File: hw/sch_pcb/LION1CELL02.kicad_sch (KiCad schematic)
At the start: 82 parts, among them IC1 BQ294602DRVR, J1 CONN1_1, J10 JUMP_2x1, J11 JUMP_2x1, J12 JUMP_2x1, J13 JUMP_2x1, J2 CONN1_1, J3 Jack-DC, J4 JUMP_2x1, J5 JUMP_2x1, J6 JUMP_2x1, J7 JUMP_2x1, J8 JUMP2_2x1, J9 Conn_02x03_Odd_Even, M1 HOLE M3, M2 HOLE M3, M3 HOLE, M4 HOLE, Q1 IRLML6244, SW1 SW_PUSH, U1 BQ24103, U2 SN74HC164D, U3 BQ34Z100

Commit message: Update schematics
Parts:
- removed BT1: lion, symbol Device:Battery_Cell
- removed C1, C14, C5: 100nF, Mlab_C:SMD-0805, symbol Device:C
- removed C10, C11, C13, C3, C4, C6, C7, C9: 100nF, Mlab_C:SMD-0805, symbol LION2CELL01D-rescue:C-RESCUE-LION2CELL01C
- removed C12: 1uF, Mlab_C:SMD-0805, symbol LION2CELL01D-rescue:C-RESCUE-LION2CELL01C
- removed C15: 100nF, Mlab_R:SMD-0805, symbol LION2CELL01D-rescue:C-RESCUE-LION2CELL01C
- removed C2: 10uF, Mlab_C:TantalC_SizeD_Reflow, symbol Device:C_Polarized
- removed C8: 10uF, Mlab_C:TantalC_SizeD_Reflow, symbol LION2CELL01D-rescue:CP2
- removed D1: M4, Mlab_D:SMA_Standard, symbol LION2CELL01D-rescue:DIODE
- removed D10, D11, D12, D13, D14, D7, D8, D9: ORAGE, Mlab_D:LED_1206, symbol LION2CELL01D-rescue:LED-RESCUE-LION2CELL01C
- removed D2: M4, symbol Device:D
- removed D3, D4: Green, Mlab_D:LED_1206, symbol LION2CELL01D-rescue:LED-RESCUE-LION2CELL01C
- removed D5: Red, Mlab_D:LED_1206, symbol LION2CELL01D-rescue:LED-RESCUE-LION2CELL01C
- removed D6: ZSMD-5V6, symbol Device:D_Zener
- removed IC1: BQ294602DRVR, symbol BQ294602DRVR:BQ294602DRVR
- removed J10, J11, J12, J13, J4, J5, J6, J7: JUMP_2x1, Mlab_Pin_Headers:Straight_1x02, symbol LION2CELL01D-rescue:JUMP_2x1
- removed J3: Jack-DC, symbol Connector:Jack-DC
- removed J8: JUMP2_2x1, symbol LION2CELL01D-rescue:JUMP2_2x1
- removed L1: DE1205-10, Mlab_L:DE1205-10, symbol LION2CELL01D-rescue:INDUCTOR_SMALL
- removed M1, M2: HOLE M3, Mlab_Mechanical:MountingHole_3mm, symbol mlab-default-rescue:HOLE
- removed M3, M4: HOLE, Mlab_Mechanical:MountingHole_3mm, symbol mlab-default-rescue:HOLE
- removed Q1: IRLML6244, Mlab_T:SOT-23, symbol LION2CELL01D-rescue:MOSFET-N
- removed R1, R7: 7k5, symbol Device:R
- removed R10: 9K31, Mlab_R:SMD-0805, symbol LION2CELL01D-rescue:R-RESCUE-LION2CELL01C
- removed R11: 442K, Mlab_R:SMD-0805, symbol LION2CELL01D-rescue:R-RESCUE-LION2CELL01C
- removed R12: 0R1, Resistors_SMD:R_2512, symbol LION2CELL01D-rescue:R-RESCUE-LION2CELL01C
- removed R13, R14, R15, R16, R17, R18, R19, R20, R4, R5, R6: 270R, Mlab_R:SMD-0805, symbol LION2CELL01D-rescue:R-RESCUE-LION2CELL01C
- removed R2, R3: 10k, Mlab_R:SMD-0805, symbol LION2CELL01D-rescue:R-RESCUE-LION2CELL01C
- removed R21: 1K, Mlab_R:SMD-0805, symbol LION2CELL01D-rescue:R-RESCUE-LION2CELL01C
- removed R22, R23: 100R, Mlab_R:SMD-0805, symbol LION2CELL01D-rescue:R-RESCUE-LION2CELL01C
- removed R24: 0R01 75PPM, Mlab_R:SMD-2512, symbol LION2CELL01D-rescue:R-RESCUE-LION2CELL01C
- removed R8, R9: 7K5, Mlab_R:SMD-0805, symbol LION2CELL01D-rescue:R-RESCUE-LION2CELL01C
- removed SW1: SW_PUSH, Mlab_SW:SW_PUSH_SMALL, symbol LION2CELL01D-rescue:SW_PUSH
- removed TH1, TH2: NCP21XV103J03RA, symbol Device:Thermistor
- removed U1: BQ24103, Mlab_IO:VQFN-20, symbol LION2CELL01D-rescue:BQ24103
- removed U2: SN74HC164D, Mlab_IO:SO-14, symbol LION2CELL01D-rescue:SN74HC164D
- removed U3: BQ34Z100, Mlab_IO:TSSOP-14_4.4x5mm_Pitch0.65mm, symbol LION2CELL01D-rescue:BQ34Z100
- added BT1: BATT, Mlab_Batery:BAT_BK-18650-PC4, symbol MLAB_BATERY:2xBATT
- added C10, C36: 22u, Capacitor_SMD:C_0805_2012Metric, symbol Device:C_Small
- added C11: 4u7, Capacitor_SMD:C_0805_2012Metric, symbol Device:C_Small
- added C18: 100n, symbol Device:C
- added C25, C26, C29, C30, C6: 100n, Capacitor_SMD:C_0805_2012Metric, symbol Device:C_Small
- added C31, C7: 1u, Capacitor_SMD:C_0805_2012Metric, symbol Device:C_Small
- added C34: 3n3, Capacitor_SMD:C_0805_2012Metric, symbol Device:C_Small
- added C39: 47u, Capacitor_SMD:C_0805_2012Metric, symbol Device:C_Small
- added C4: 100nF, Capacitor_SMD:C_0805_2012Metric, symbol Device:C_Small
- added C42, C5, C9: 10u, Capacitor_SMD:C_0805_2012Metric, symbol Device:C_Small
- added C53: 1n, Capacitor_SMD:C_0805_2012Metric, symbol Device:C_Small
- added C8: 47n, Capacitor_SMD:C_0805_2012Metric, symbol Device:C_Small
- added D1, D4, D5: ORANGE, Mlab_D:SMD_LED_RIGHT_KINGBRIGHT_1605, symbol Device:LED_Small
- added D10, D6, D7, D8, D9: GREEN, Mlab_D:SMD_LED_RIGHT_KINGBRIGHT_1605, symbol Device:LED_Small
- added D2, D3: RED, Mlab_D:SMD_LED_RIGHT_KINGBRIGHT_1605, symbol Device:LED_Small
- added FID1, FID2, FID3, FID4: Fiducial, Fiducial:Fiducial_1mm_Mask2mm, symbol Mechanical:Fiducial
- added H1, H2, H3, H4: M3, Mlab_Mechanical:MountingHole_3mm, symbol Mechanical:MountingHole_Pad
- added J1: USBC_USB4105-GF-A, Mlab_CON:USBC GCT_USB4105-GF-A, symbol MLAB_CONNECTORS:USBC_USB4105-GF-A
- added J9: JUMP_4X2, symbol MLAB_Jumpers:JUMP_4X2
- added JP5: Jumper_3_Bridged12, Jumper:SolderJumper-3_P1.3mm_Bridged2Bar12_RoundedPad1.0x1.5mm, symbol Jumper:SolderJumper_3_Bridged12
- added L1, L2: 1uH - DFE252012P-1R0M=P2, Inductor_SMD:L_1008_2520Metric, symbol Device:L
- added NT1, NT2: NetTie_2, NetTie:NetTie-2_SMD_Pad0.5mm, symbol Device:NetTie_2
- added Q1, Q2: DMN1029UFDB-7, symbol Transistor_FET:Q_NMOS_GDS
- added Q4: BSS83P, Package_TO_SOT_SMD:SOT-23, symbol Device:Q_PMOS_GSD
- added Q5, Q6: BC807-25, Package_TO_SOT_SMD:SOT-23-3, symbol Device:Q_PNP_BEC
- added R1, R2, R21: 5k1, Resistor_SMD:R_0805_2012Metric, symbol Device:R_Small
- added R10, R11, R12, R13, R19, R50: 270R, Resistor_SMD:R_0805_2012Metric, symbol Device:R_Small
- added R14, R15, R16, R17, R51: 68R, Resistor_SMD:R_0805_2012Metric, symbol Device:R_Small
- added R18: 2k4, Resistor_SMD:R_0805_2012Metric, symbol Device:R_Small
- added R20, R48, R49: 1k, Resistor_SMD:R_0805_2012Metric, symbol Device:R_Small
- added R22: 33k, Resistor_SMD:R_0805_2012Metric, symbol Device:R_Small
- added R27: 330, symbol Device:R
- added R28: 2k2, symbol Device:R
- added R3: 0R01 75PPM, Resistor_SMD:R_2512_6332Metric, symbol Device:R_Small
- added R5, R6: 4M7, Resistor_SMD:R_0805_2012Metric, symbol Device:R_Small
- added R59, R60: 100R, Resistor_SMD:R_0805_2012Metric, symbol Device:R_Small
- added R75: 511k, Resistor_SMD:R_0805_2012Metric, symbol Device:R_Small
- added R76: 91k, Resistor_SMD:R_0805_2012Metric, symbol Device:R_Small
- added R8: R, Resistor_SMD:R_0805_2012Metric, symbol Device:R_Small
- added R9: 510R, Resistor_SMD:R_0805_2012Metric, symbol Device:R_Small
- added SW3: SKRTLAE010, Mlab_SW:SKRT, symbol MLAB_SW:SW_Push_shield
- added TH1: 10k NTC, Resistor_SMD:R_0805_2012Metric, symbol Device:Thermistor_NTC
- added TH3: 10k NTC, Resistor_SMD:R_0805_2012Metric, symbol Device:Thermistor
- added U1: BQ29700DSER, Package_SON:WSON-6_1.5x1.5mm_P0.5mm, symbol Battery_Management:BQ297xy
- added U15: TPS631000DRLR, Package_TO_SOT_SMD:SOT-583-8, symbol MLAB_U:TPS631000DRLR
- added U2: SN74HC164P, Package_SO:TSSOP-14_4.4x5mm_P0.65mm, symbol MLAB_IO:SN74HC164D
- added U3: BQ25628E, Mlab_IO:Texas_S-WQFN-HR-18, symbol MLAB_IO:BQ25628E
- added U5: BQ34Z100, Mlab_IO:TSSOP-14_4.4x5mm_Pitch0.65mm, symbol MLAB_IO:BQ34Z100
- F1: value 3A -> Fuse; footprint (none) -> Fuse:Fuseholder_Littelfuse_Nano2_154x; UST_ID (none) -> 5c70984512875079b91f88d8
- F2: value 1.1A -> Fuse; footprint (none) -> Fuse:Fuseholder_Littelfuse_Nano2_154x; UST_ID (none) -> 5c70984512875079b91f88d8
- renumbered J1 to J2, J2 to J3, J9 to J4
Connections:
- net BAT+: no longer F1.2
- net GND: now also C10.2, C11.2, C18.2, C25.2, C29.2, C30.2, C31.2, C34.2, C36.2, C39.2, C4.2, C42.2, C5.2, C53.2, C6.2, C7.2, C9.2, D1.1 (K), D10.1 (K), H1.1, H2.1, H3.1, H4.1, J1.A1/B12 (GND), J1.B1/A12 (GND), J1.G1 (SHIELD), J1.G2 (SHIELD), J1.G3 (SHIELD), J1.G4 (SHIELD), J9.1 (2), J9.2, NT2.2, Q2.3 (S), R1.1, R18.2, R2.1, R20.1, R28.2, R3.2, R6.1, R76.2, U1.4 (VSS), U15.6 (MODE), U15.7 (GND), U2.7 (GND), U3.14 (~{CE}), U3.15 (GND), U5.8 (VSS)
- net HDQ: now also J9.3 (4), J9.4, U5.12 (P5/HDQ)
- net P1: now also U2.1 (A), U2.2 (B), U5.3 (P1)
- net P2: now also U2.8 (CLK), U5.1 (P2)
- net SCL: now also J9.5, J9.6 (5), U3.13 (SCL), U5.13 (P4/SCL)
- net SDA: now also J9.7 (8), J9.8, U3.12 (SDA), U5.14 (P3/SDA)
- net at F2.2: now also BT1.2+ (+)
- net +BATT: now reaches F2.1
- net +BATT: now also F1.1, C34.1, C9.1, JP5.3 (B), Q1.3 (S), R27.1, R5.1, U3.8 (BAT), U5.4 (BAT)
- new net: J1.B5 (CC2), R1.2
- new net: D6.1 (K), R14.1
- new net: C26.2, C30.1, R60.2, U5.10 (SRN)
- new net: Q5.3 (C), R51.1
- new net: D10.2 (A), R51.2
- new net: D7.1 (K), R15.1
- new net: BT1.1+ (+), F1.2
- new net: Q5.1 (B), R49.2
- new net: C25.1, JP5.2 (C), U5.5 (CE), U5.6 (REGIN)
- new net: D9.1 (K), R17.1
- new net: C7.1, R18.1, U3.4 (ILIM)
- new net: L2.1, U15.3 (LX1)
- new net: L2.2, U15.2 (LX2)
- new net: C8.1, L1.1, U3.16 (SW)
- new net: C8.2, U3.1 (BTST)
- new net: C26.1, C29.1, R59.2, U5.9 (SRP)
- new net: R21.1, U3.5 (TS_BIAS)
- new net: R21.2, R22.1, TH1.1, U3.6 (TS)
- new net: Q2.1 (G), R6.2, U1.3 (Dout)
- new net: C31.1, TH3.1, U5.7 (REG25)
- new net: Q1.1 (G), R5.2, U1.2 (Cout)
- new net: Q1.2 (D), Q2.2 (D)
- new net: Q6.1 (B), R48.2
- new net: TH3.2, U5.11 (P6/TS)
- new net: Q4.1 (G), R9.2
- new net: Q4.3 (D), R19.2
- new net: D5.1 (K), R13.1
- new net: C18.1, R27.2, U1.5 (BAT)
- new net: D4.1 (K), R12.1
- new net: D2.1 (K), R10.1
- new net: R28.1, U1.6 (V-)
- new net: J1.A5 (CC1), R2.2
- new net: R22.2, TH1.2
- new net: D3.1 (K), R11.1
- new net: C5.1, C6.1, U3.17 (PMID)
- new net: C11.1, U3.2 (REGN)
- new net: D1.2 (A), R50.2
- new net: J1.A6 (D+), J1.B6 (D+)
- new net: D8.1 (K), R16.1
- new net: Q6.3 (C), R50.1
- new net +3.3V: C39.1, C4.1, C42.1, D2.2 (A), D3.2 (A), D4.2 (A), D5.2 (A), D6.2 (A), D7.2 (A), D8.2 (A), D9.2 (A), JP5.1 (A), Q4.2 (S), Q5.2 (E), Q6.2 (E), R75.1, R8.2, U15.1 (VOUT), U2.14 (VCC), U2.9 (CLR)
- new net +VSW: C10.1, C36.1, L1.2, U15.4 (VIN), U15.5 (EN), U3.9 (SYS)
- new net 3v3i_FB: R75.2, R76.1, U15.8 (FB)
- new net A: R10.2, U2.3 (QA)
- new net B: R11.2, U2.4 (QB)
- new net BAT-: BT1.1- (-), BT1.2- (-), NT1.2, R3.1
- new net C: R12.2, U2.5 (QC)
- new net CH_PG: R49.1, U3.3 (~{PG})
- new net CH_STAT: R48.1, U3.10 (STAT)
- new net D: R13.2, U2.6 (QD)
- new net E: R14.2, U2.10 (QE)
- new net EXT_DETECTION_CHARGER: R8.1, R9.1, SW3.1, U3.7 (~{QON})
- new net F: R15.2, U2.11 (QF)
- new net G: R16.2, U2.12 (QG)
- new net GAUGE_BTN_IN: R19.1, R20.2, U5.2 (VEN)
- new net GAUGE_SRN: NT2.1, R60.1
- new net GAUGE_SRP: NT1.1, R59.1
- new net H: R17.2, U2.13 (QH)
- new net VBUS: C53.1, J1.A4/B9 (VBUS), J1.B4/A9 (VBUS), U3.18 (VBUS)
- no-connect marks 0 -> 3
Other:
- note added: "+3.3V"
- note added: "0%"
- note added: "100%"
- note added: "GREEN"
- note added: "Need to obtain 2.5V, here"
- note added: "ORANGE"
- note added: "RED"
- note removed: "MOUNTING HOLES"
- note removed: "TO HOST MCU"
- moved on the sheet: J2, J3, J4

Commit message: Update schematics
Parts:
- removed C18: 100n, symbol Device:C
- removed J2, J3: CONN1_1, Mlab_Con:WAGO256, symbol LION2CELL01D-rescue:CONN1_1
- removed J4: Conn_02x03_Odd_Even, symbol Connector_Generic:Conn_02x03_Odd_Even
- removed J9: JUMP_4X2, symbol MLAB_Jumpers:JUMP_4X2
- removed R27: 330, symbol Device:R
- removed R8: R, Resistor_SMD:R_0805_2012Metric, symbol Device:R_Small
- removed SW3: SKRTLAE010, Mlab_SW:SKRT, symbol MLAB_SW:SW_Push_shield
- added C7: 100n, Capacitor_SMD:C_0805_2012Metric, symbol Device:C_Small
- added J2: HEADER_2x03, Connector_PinHeader_2.54mm:PinHeader_2x03_P2.54mm_Vertical, symbol MLAB_HEADER:HEADER_2x03
- added J3: HEADER_1x04, Connector_PinHeader_2.54mm:PinHeader_1x04_P2.54mm_Horizontal, symbol MLAB_HEADER:HEADER_1x04
- added R11: 330, symbol Device:R_Small
- added R30, R31: 4k7, Resistor_SMD:R_0805_2012Metric, symbol Device:R_Small
- added SW1: SKRTLAE010, Mlab_SW:SKRT, symbol MLAB_SW:SW_Push_shield
- C13: renamed from C4; value 100nF -> 100n
- R12: renamed from R28; footprint (none) -> Resistor_SMD:R_0805_2012Metric
- renumbered C36 to C1, C9 to C10, C10 to C11, C11 to C12, C25 to C14, C26 to C15, C29 to C16, C30 to C17, C31 to C18, C34 to C19, C39 to C2, C53 to C3, C42 to C4, C7 to C8, C8 to C9, D9 to D10, D10 to D2, D2 to D3, D3 to D4, D4 to D5, D5 to D6, D6 to D7, D7 to D8, D8 to D9, JP5 to JP1, L2 to L1, L1 to L2, Q6 to Q1, Q5 to Q2, Q4 to Q3, Q1 to Q4, Q2 to Q5, R9 to R10, R19 to R13, R20 to R14, R18 to R15, R21 to R16, R22 to R17, R5 to R18, R6 to R19, R10 to R20, R11 to R21, R12 to R22, R13 to R23, R14 to R24, R15 to R25, R16 to R26, R17 to R27, R59 to R28, R60 to R29, R75 to R3, R76 to R4, R48 to R5, R49 to R6, R50 to R7, R51 to R8, R3 to R9, TH3 to TH2, U15 to U1, U3 to U2, U1 to U3, U5 to U4, U2 to U5
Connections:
- net +3.3V: now also J3.4, R30.2, R31.2
- net +BATT: now also J2.3, J2.4, R11.1
- net GND: now also C7.2, J2.1, J2.2, J2.5, J2.6, J3.1, SW1.2, SW1.GND (SHIELD)
- net SCL: now also J3.3, R30.1
- net SDA: now also J3.2, R31.1
- net at U3.5 (BAT): now also C7.1, R11.2
- net at J1.A6 (D+): no longer J1.B6 (D+)
- net EXT_DETECTION_CHARGER renamed RESET
- net RESET: now also SW1.1
- net HDQ: no longer names the net of U4.12 (P5/HDQ)
- no-connect marks 3 -> 8
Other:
- note added: "BUCK CONVERTER"
- note added: "I2C"
- note added: "MOUNTING HOLES"
- note added: "POWER OUT"
- note added: "UI"
- note added: "USB-C"
- note removed: "POWER OUTPUT"
- moved on the sheet: BT1A, BT1B, C1, C10, C11, C12, C13, C14, C15, C16, C17, C18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

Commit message: Repository cleanup.
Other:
- company: Mlab.cz -> MLAB.cz
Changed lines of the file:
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@@
 		(title "LION1CELL02A")
 		(date "2024-07-17")
-		(company "Mlab.cz")
+		(company "MLAB.cz")
 		(comment 1 "Singe cell Li-ion battery management\\nwith USB-C charger")
 	)

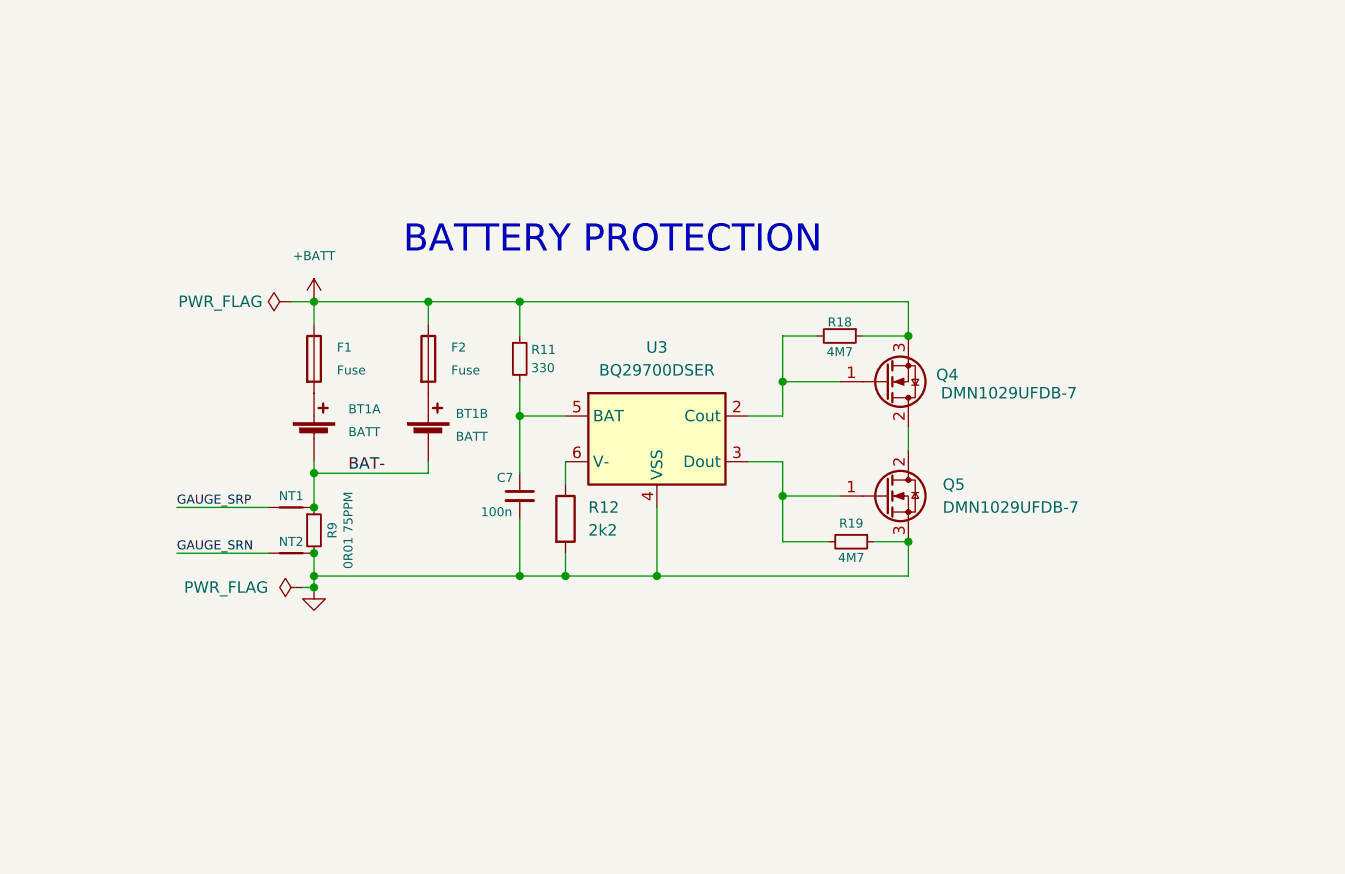
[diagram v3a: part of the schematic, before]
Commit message: Batery protection update
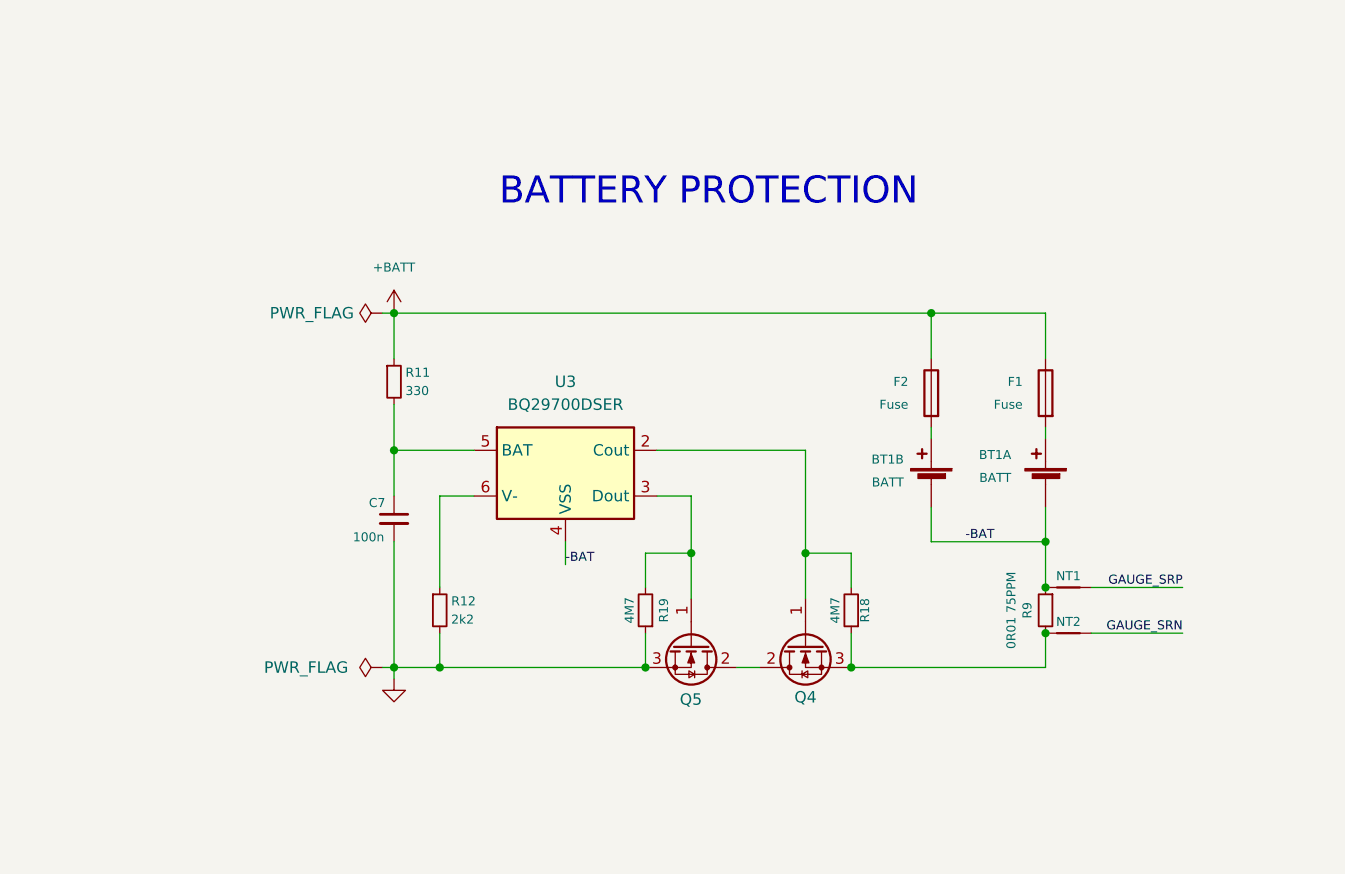
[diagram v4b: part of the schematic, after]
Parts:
- removed R12: 2k2, Resistor_SMD:R_0805_2012Metric, symbol Device:R
- added R12: 2k2, symbol Device:R_Small
- Q4, Q5: value DMN1029UFDB-7 -> ~
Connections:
- net +BATT: no longer Q4.3 (S), R18.1
- net GND: now also R12.2; no longer NT2.2, R9.2, U3.4 (VSS)
- net at U3.6 (V-): now also R12.1
- net BAT- renamed -BAT
- net -BAT: now also U3.4 (VSS)
- new net: NT2.2, Q4.3 (S), R18.1, R9.2
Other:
- moved on the sheet: BT1A, BT1B, C7, F1, F2, NT1, NT2, Q4, Q5, R11, R18, R19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

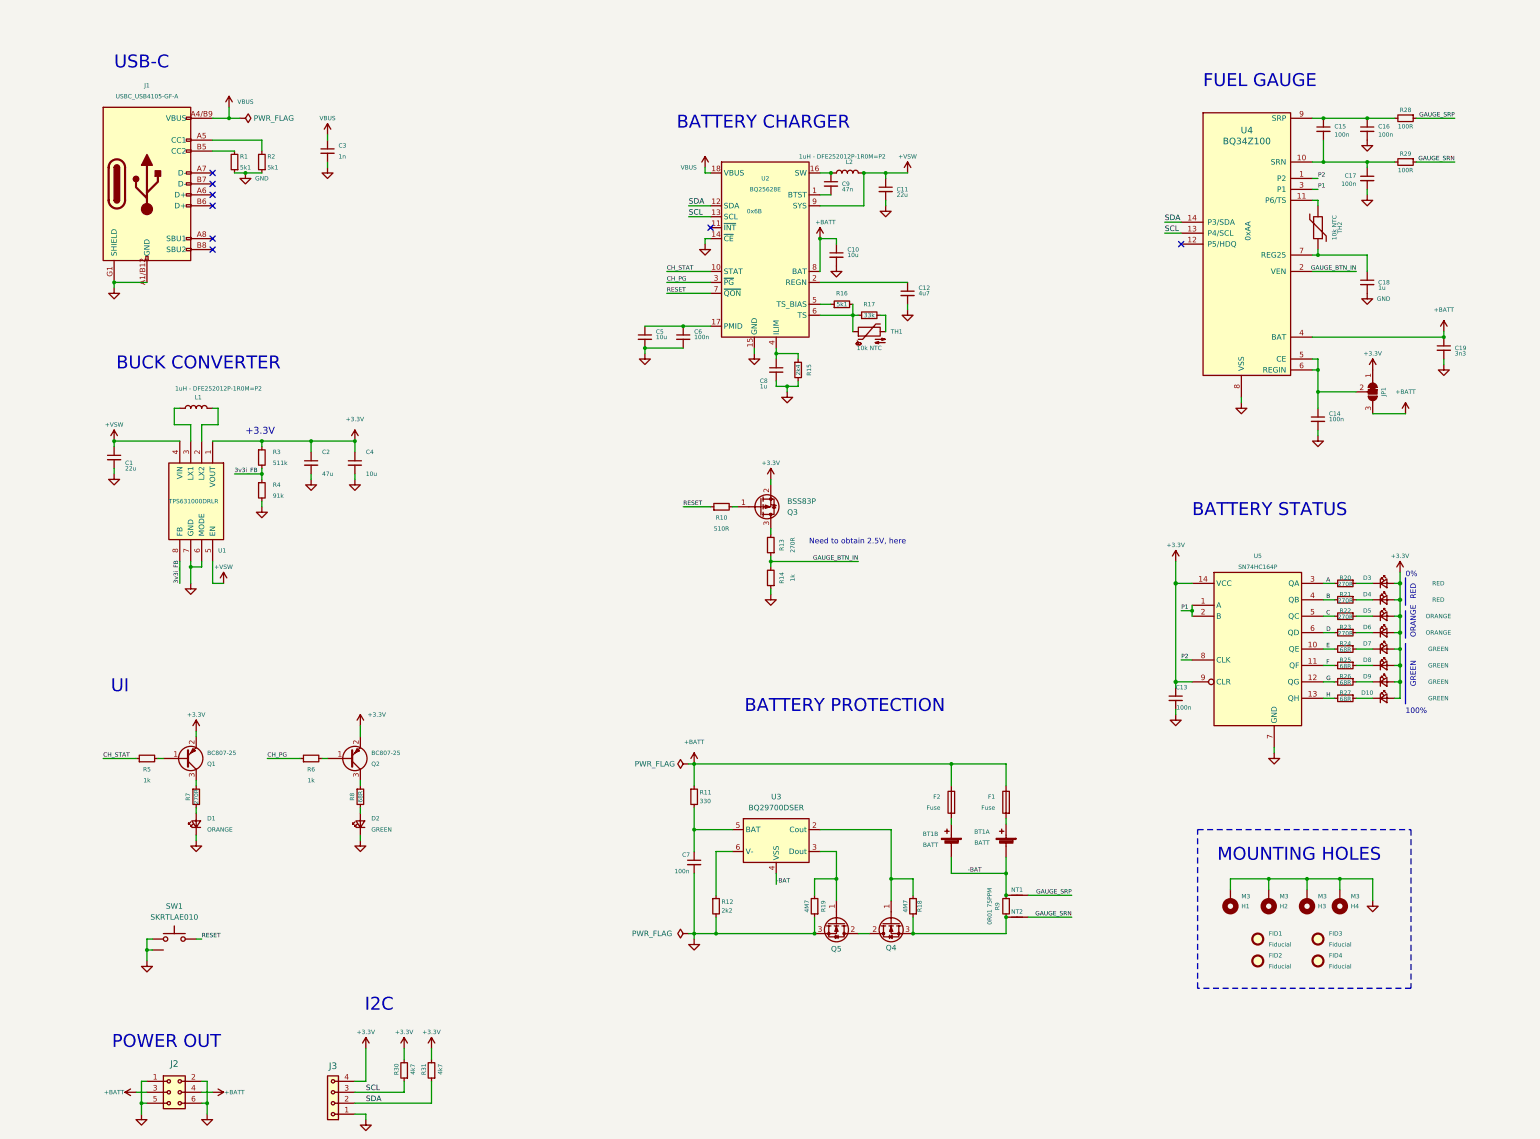
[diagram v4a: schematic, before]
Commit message: Battery pack update
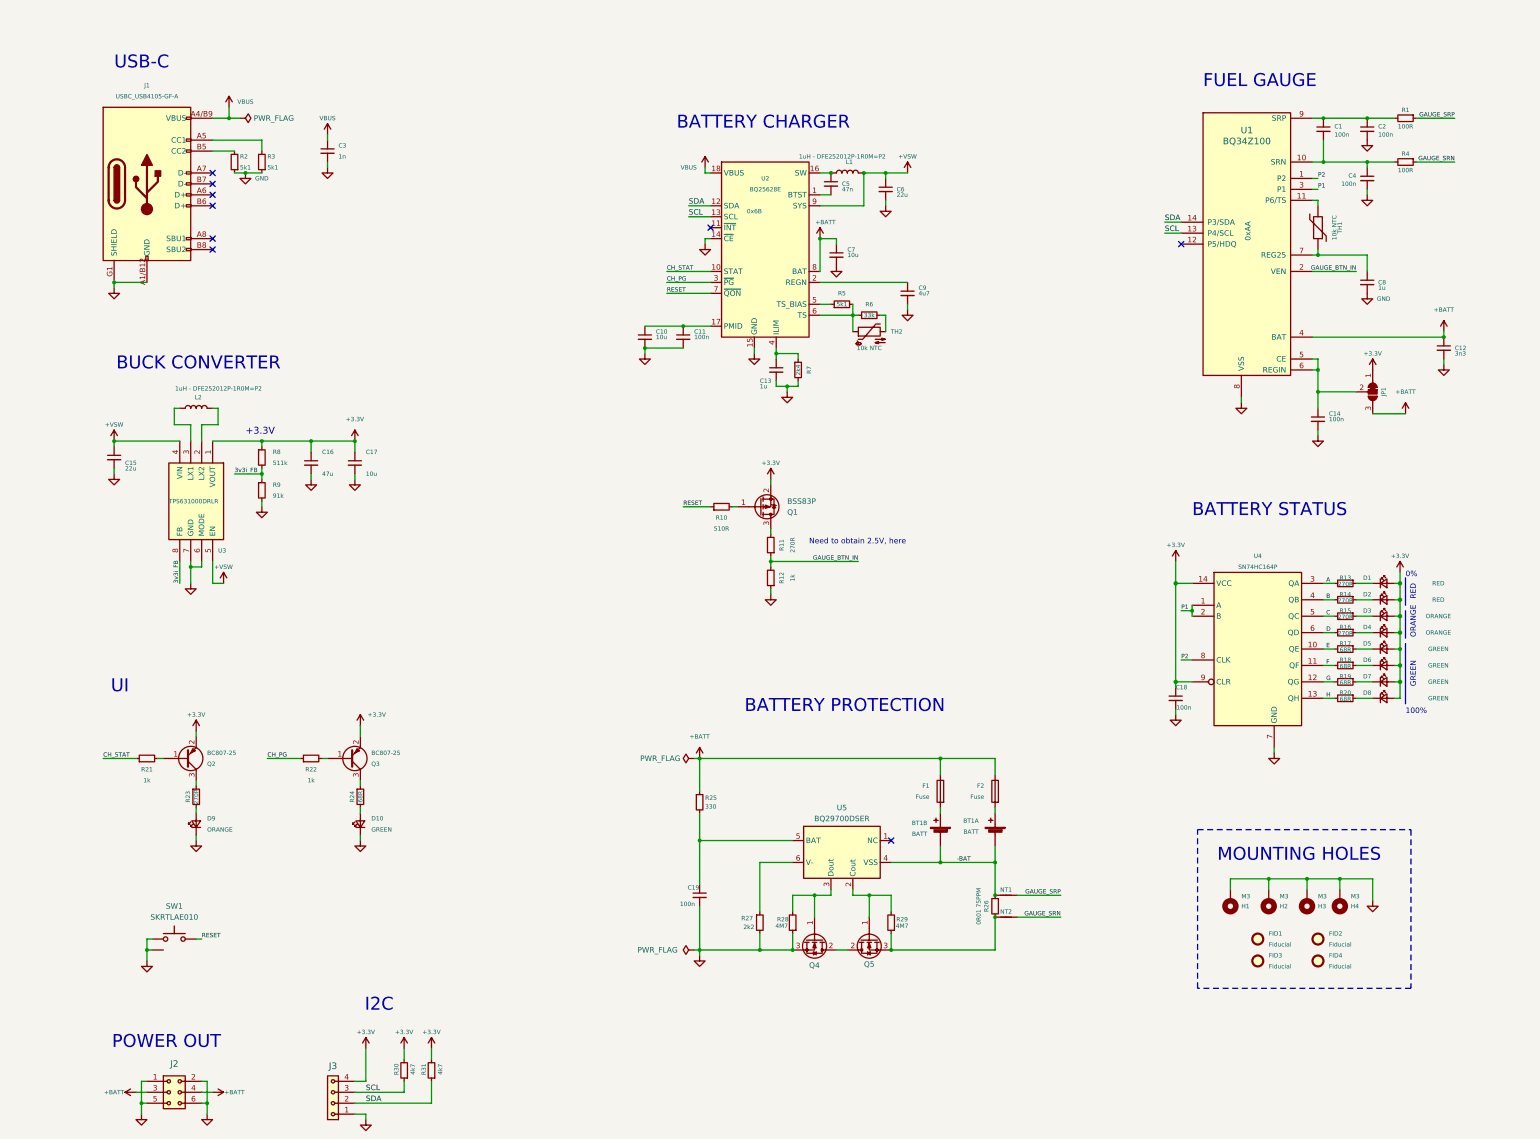
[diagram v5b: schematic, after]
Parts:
- renumbered C15 to C1, C5 to C10, C6 to C11, C19 to C12, C8 to C13, C1 to C15, C2 to C16, C4 to C17, C13 to C18, C7 to C19, C16 to C2, C17 to C4, C9 to C5, C11 to C6, C10 to C7, C18 to C8, C12 to C9, D3 to D1, D2 to D10, D4 to D2, D5 to D3, D6 to D4, D7 to D5, D8 to D6, D9 to D7, D10 to D8, D1 to D9, F2 to F1, F1 to F2, FID3 to FID2, FID2 to FID3, L2 to L1, L1 to L2, Q3 to Q1, Q1 to Q2, Q2 to Q3, Q5 to Q4, Q4 to Q5, R28 to R1, R13 to R11, R14 to R12, R20 to R13, R21 to R14, R22 to R15, R23 to R16, R24 to R17, R25 to R18, R26 to R19, R1 to R2, R27 to R20, R5 to R21, R6 to R22, R7 to R23, R8 to R24, R11 to R25, R9 to R26, R12 to R27, R19 to R28, R18 to R29, R2 to R3, R29 to R4, R16 to R5, R17 to R6, R15 to R7, R3 to R8, R4 to R9, TH2 to TH1, TH1 to TH2, U4 to U1, U1 to U3, U5 to U4, U3 to U5
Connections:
- no-connect marks 8 -> 9
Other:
- moved on the sheet: BT1A, BT1B, C19, F1, F2, NT1, NT2, Q4, Q5, R25, R26, R27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
